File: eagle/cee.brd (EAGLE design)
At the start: 50 x 80 mm, 51 parts, among them IC1 IC1, J1 SOLDERJUMPERNC2

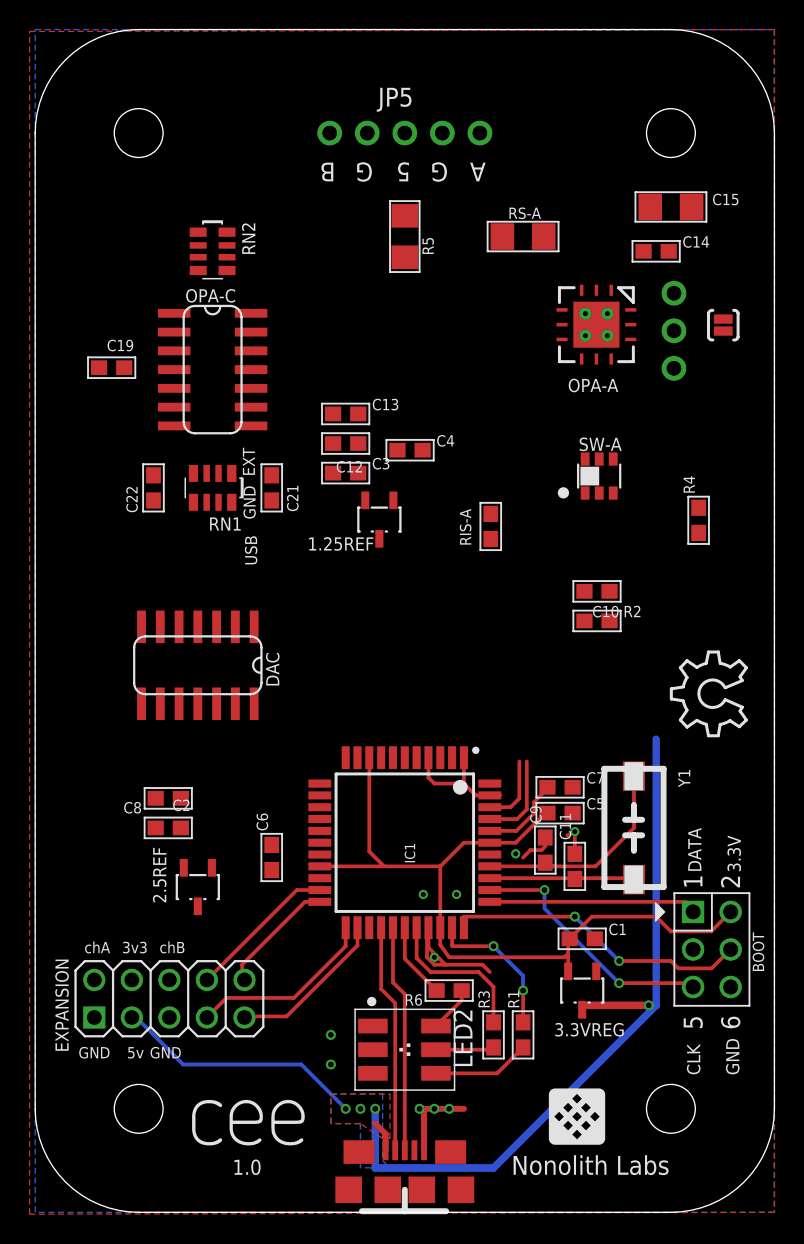
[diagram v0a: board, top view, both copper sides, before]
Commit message: Move output header 1mm inward so it doesn't go beyond acrylic.
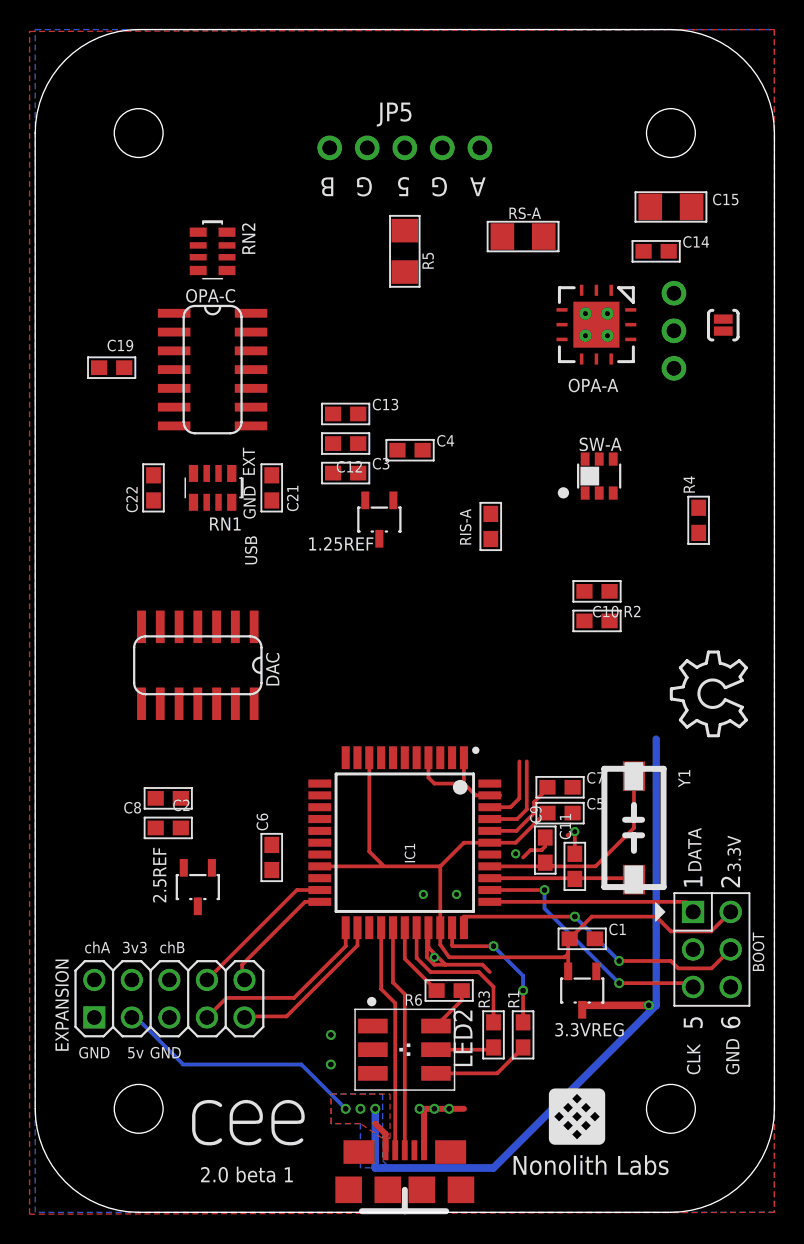
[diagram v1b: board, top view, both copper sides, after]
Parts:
- moved JP5 1.00 mm to (25.0, 72.0)
- moved R5 1.00 mm to (25.0, 65.0)
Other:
- board text added: "2.0 beta 1"
- board text removed: "1.0"
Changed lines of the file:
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@@
 <text x="36.0238" y="55.482" size="0.889" layer="25" font="vector" ratio="12">OPA-A</text>
 <text x="32.2072" y="2.54" size="1.27" layer="25" font="vector" ratio="12">Nonolith Labs</text>
-<text x="20.32" y="71" size="1.27" layer="25" font="vector" ratio="12" rot="SR180">B</text>
-<text x="30.48" y="71" size="1.27" layer="25" font="vector" ratio="12" rot="SR180">A</text>
+<text x="20.32" y="70" size="1.27" layer="25" font="vector" ratio="12" rot="SR180">B</text>
+<text x="30.48" y="70" size="1.27" layer="25" font="vector" ratio="12" rot="SR180">A</text>
 <text x="14.859" y="49.784" size="0.8128" layer="21" rot="R90">EXT</text>
 <text x="15.0114" y="43.7388" size="0.8128" layer="21" rot="R90">USB</text>
@@
 <text x="5.08" y="11.176" size="0.762" layer="25" font="vector" ratio="11" rot="R180">GND</text>
 <text x="7.366" y="11.176" size="0.762" layer="25" font="vector" ratio="11" rot="R180">5v</text>
-<text x="13.335" y="2.54" size="1.016" layer="25" font="vector" ratio="12">1.0</text>
-<text x="22.86" y="71" size="1.27" layer="25" font="vector" ratio="12" rot="SR180">G</text>
-<text x="25.4" y="71" size="1.27" layer="25" font="vector" ratio="12" rot="SR180">5</text>
-<text x="27.94" y="71" size="1.27" layer="25" font="vector" ratio="12" rot="SR180">G</text>
+<text x="14.335" y="2.54" size="1.016" layer="25" font="vector" ratio="12" align="center">2.0 beta 1</text>
+<text x="22.86" y="70" size="1.27" layer="25" font="vector" ratio="12" rot="SR180">G</text>
+<text x="25.4" y="70" size="1.27" layer="25" font="vector" ratio="12" rot="SR180">5</text>
+<text x="27.94" y="70" size="1.27" layer="25" font="vector" ratio="12" rot="SR180">G</text>
 <text x="9.906" y="11.176" size="0.762" layer="25" font="vector" ratio="11" rot="R180">GND</text>
 </plain>
@@
 <attribute name="NAME" x="14" y="67" size="0.889" layer="25" font="vector" ratio="12" rot="R270"/>
 </element>
-<element name="JP5" library="nonolith" package="1X05_ROUND" value="" x="25" y="73" smashed="yes" rot="R180">
-<attribute name="NAME" x="23.1838" y="74.7928" size="1.27" layer="25" ratio="10"/>
-<attribute name="VALUE" x="31.35" y="76.175" size="1.27" layer="27" rot="R180"/>
-</element>
-<element name="R5" library="nonolith" package="1206" value="15o" x="25" y="66" smashed="yes" rot="R90">
-<attribute name="NAME" x="26.9558" y="64.73" size="0.762" layer="25" font="vector" ratio="10" rot="R90"/>
+<element name="JP5" library="nonolith" package="1X05_ROUND" value="" x="25" y="72" smashed="yes" rot="R180">
+<attribute name="NAME" x="23.1838" y="73.7928" size="1.27" layer="25" ratio="10"/>
+<attribute name="VALUE" x="31.35" y="75.175" size="1.27" layer="27" rot="R180"/>
+</element>
+<element name="R5" library="nonolith" package="1206" value="15o" x="25" y="65" smashed="yes" rot="R90">
+<attribute name="NAME" x="26.9558" y="63.73" size="0.762" layer="25" font="vector" ratio="10" rot="R90"/>
 </element>
 <element name="CN1" library="nonolith" package="USB-MICROB" value="" x="25" y="1.524"/>
@@
 <contactref element="RN2" pad="1"/>
 <contactref element="JP5" pad="1"/>
-<wire x1="31.6" y1="66" x2="30.08" y2="73" width="0" layer="19" extent="1-1"/>
-<wire x1="11.025" y1="66.295" x2="30.08" y2="73" width="0" layer="19" extent="1-1"/>
+<wire x1="31.6" y1="66" x2="30.08" y2="72" width="0" layer="19" extent="1-1"/>
+<wire x1="11.025" y1="66.295" x2="30.08" y2="72" width="0" layer="19" extent="1-1"/>
 <wire x1="11.025" y1="65.4" x2="11.025" y2="66.295" width="0" layer="19" extent="1-1"/>
 <wire x1="3.997" y1="15.718" x2="11.025" y2="65.4" width="0" layer="19" extent="1-1"/>
@@
 <contactref element="RN2" pad="3"/>
 <contactref element="JP5" pad="5"/>
-<wire x1="11.025" y1="64.6" x2="19.92" y2="73" width="0" layer="19" extent="1-1"/>
+<wire x1="11.025" y1="64.6" x2="19.92" y2="72" width="0" layer="19" extent="1-1"/>
 <wire x1="9.077" y1="15.718" x2="11.025" y2="64.6" width="0" layer="19" extent="1-1"/>
 </signal>
@@
 <wire x1="43.2052" y1="62.165" x2="40.285" y2="61.04" width="0" layer="19" extent="1-1"/>
 <wire x1="46.542" y1="60.4187" x2="43.2052" y2="62.165" width="0" layer="19" extent="1-1"/>
-<wire x1="25" y1="64.6" x2="38.96" y2="62.365" width="0" layer="19" extent="1-1"/>
+<wire x1="25" y1="63.6" x2="38.96" y2="62.365" width="0" layer="19" extent="1-1"/>
 </signal>
 <signal name="BOOTLOAD">
@@
 <contactref element="JP5" pad="3"/>
 <contactref element="R5" pad="2"/>
-<wire x1="25" y1="67.4" x2="25" y2="73" width="0" layer="19" extent="1-1"/>
+<wire x1="25" y1="66.4" x2="25" y2="72" width="0" layer="19" extent="1-1"/>
 </signal>
 <signal name="N$3">

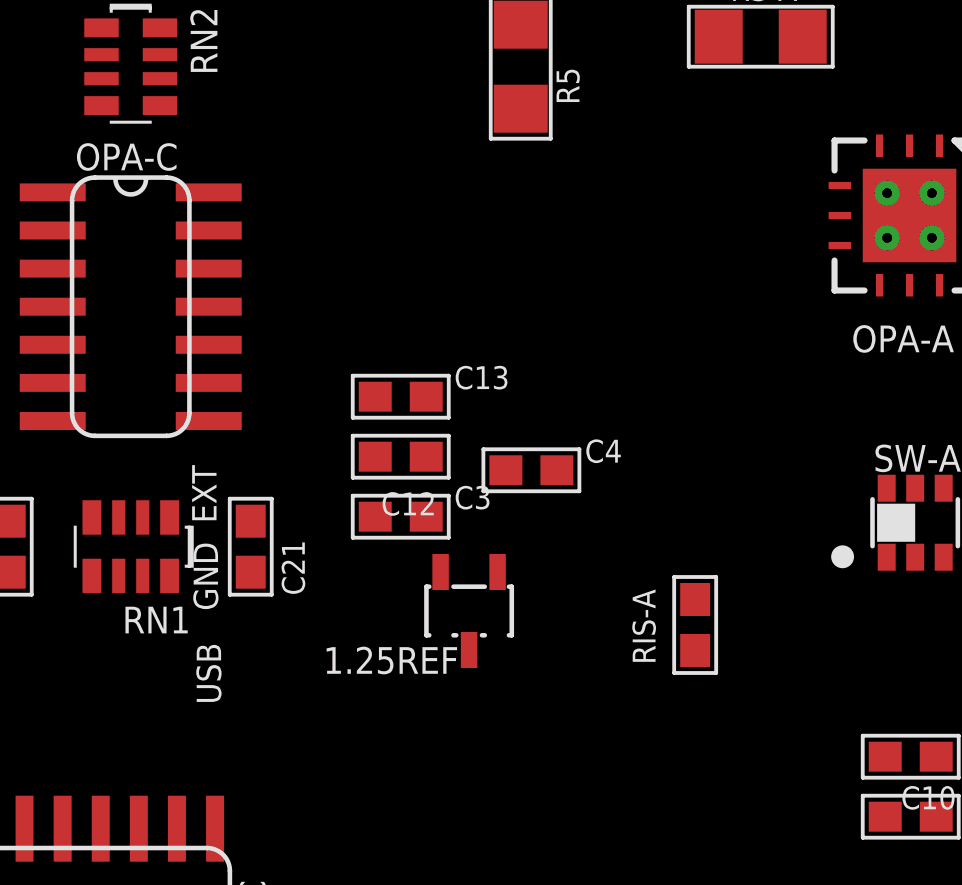
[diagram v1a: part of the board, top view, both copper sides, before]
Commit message: added INA21x
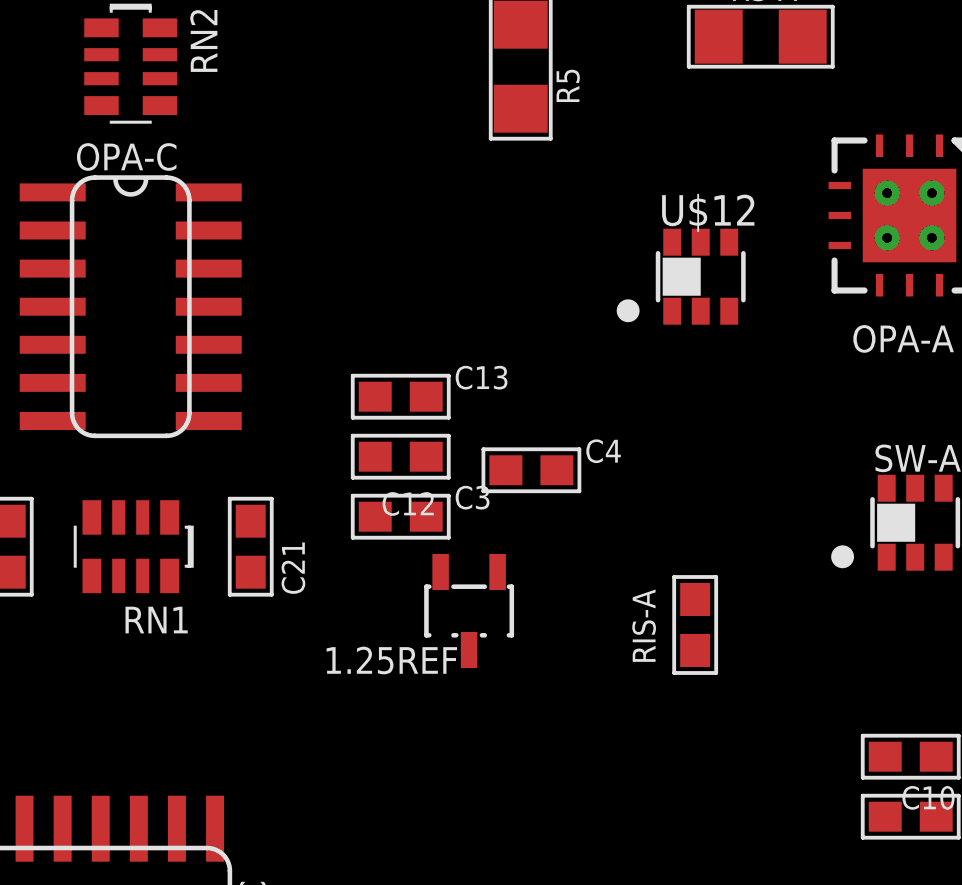
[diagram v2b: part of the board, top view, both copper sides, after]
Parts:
- added U$12: INA213, nonolith:SOT23-6
- C10: value 1nF -> DNI
- R2: value 10ko -> DNI
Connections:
- new net N$13: JP5.5
- net 1.25VREF: now also U$12.1
- net 5V: now also U$12.3
- net GND: now also U$12.2
- net SMU-A: now also U$12.4
- net SMU-B: no longer JP5.5
- net VO-A: now also U$12.5
- net VS-A: now also U$12.6
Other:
- board text removed: "EXT"
- board text removed: "USB"
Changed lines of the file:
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@@
 <?xml version="1.0" encoding="utf-8"?>
 <!DOCTYPE eagle SYSTEM "eagle.dtd">
-<eagle version="6.1">
+<eagle version="6.3">
 <drawing>
 <settings>
@@
 <text x="20.32" y="70" size="1.27" layer="25" font="vector" ratio="12" rot="SR180">B</text>
 <text x="30.48" y="70" size="1.27" layer="25" font="vector" ratio="12" rot="SR180">A</text>
-<text x="14.859" y="49.784" size="0.8128" layer="21" rot="R90">EXT</text>
-<text x="15.0114" y="43.7388" size="0.8128" layer="21" rot="R90">USB</text>
-<text x="14.9098" y="46.863" size="0.8128" layer="21" rot="R90">GND</text>
 <text x="47.625" y="9.271" size="0.889" layer="25" font="vector" ratio="12" rot="R90">GND</text>
 <text x="44.9834" y="9.271" size="0.889" layer="25" font="vector" ratio="12" rot="R90">CLK</text>
@@
 </class>
 </classes>
-<designrules>
+<designrules name="default">
 <description language="de">&lt;b&gt;EAGLE Design Rules&lt;/b&gt;
 &lt;p&gt;
@@
 <attribute name="VALUE" x="35.0188" y="12.1298" size="0.762" layer="27" ratio="12"/>
 </element>
-<element name="R2" library="nonolith" package="0603" value="10ko" x="38" y="40"/>
-<element name="C10" library="nonolith" package="0603" value="1nF" x="38" y="42" smashed="yes" rot="R180">
+<element name="R2" library="nonolith" package="0603" value="DNI" x="38" y="40"/>
+<element name="C10" library="nonolith" package="0603" value="DNI" x="38" y="42" smashed="yes" rot="R180">
 <attribute name="NAME" x="37.6698" y="40.2474" size="0.762" layer="25" font="vector" ratio="10"/>
 </element>
@@
 <element name="R3" library="nonolith" package="0603" value="0" x="31" y="12" rot="R90"/>
 <element name="R6" library="nonolith" package="0603" value="0" x="28" y="15" rot="R180"/>
+<element name="U$12" library="nonolith" package="SOT23-6" value="INA213" x="31" y="58"/>
 </elements>
 <signals>
@@
 <wire x1="10" y1="10" x2="18" y2="10" width="0.254" layer="16"/>
 <wire x1="18" y1="10" x2="21" y2="7" width="0.254" layer="16"/>
+<contactref element="U$12" pad="3"/>
 <wire x1="43.2052" y1="57.085" x2="46.542" y2="59.6051" width="0" layer="19" extent="1-1"/>
 <wire x1="38.148" y1="50.949" x2="43.2052" y2="57.085" width="0" layer="19" extent="1-1"/>
-<wire x1="24.505" y1="51.548" x2="38.148" y2="50.949" width="0" layer="19" extent="1-1"/>
+<wire x1="31.95" y1="56.85" x2="38.148" y2="50.949" width="0" layer="19" extent="1-1"/>
+<wire x1="24.505" y1="51.548" x2="31.95" y2="56.85" width="0" layer="19" extent="1-1"/>
 <wire x1="24.229" y1="48.1574" x2="24.505" y2="51.548" width="0" layer="19" extent="1-1"/>
 <wire x1="14.81" y1="39.6" x2="24.229" y2="48.1574" width="0" layer="19" extent="1-1"/>
@@
 <contactref element="JP5" pad="4"/>
 <contactref element="EXPANSION" pad="5"/>
-<contactref element="C4" pad="1"/>
 <polygon width="0.4064" layer="16" isolate="0.3048" rank="3">
 <vertex x="0" y="80"/>
@@
 <via x="26.25" y="21.5" extent="1-16" drill="0.3302" shape="octagon"/>
 <via x="28.5" y="21.5" extent="1-16" drill="0.3302" shape="octagon"/>
+<contactref element="U$12" pad="2"/>
+<contactref element="C4" pad="1"/>
 </signal>
 <signal name="PDI-DATA">
@@
 <contactref element="RN2" pad="1"/>
 <contactref element="JP5" pad="1"/>
+<contactref element="U$12" pad="4"/>
 <wire x1="31.6" y1="66" x2="30.08" y2="72" width="0" layer="19" extent="1-1"/>
+<wire x1="31.95" y1="59.15" x2="31.6" y2="66" width="0" layer="19" extent="1-1"/>
 <wire x1="11.025" y1="66.295" x2="30.08" y2="72" width="0" layer="19" extent="1-1"/>
 <wire x1="11.025" y1="65.4" x2="11.025" y2="66.295" width="0" layer="19" extent="1-1"/>
@@
 <contactref element="RS-A" pad="1"/>
 <contactref element="C10" pad="2"/>
+<contactref element="U$12" pad="5"/>
 <wire x1="37.96" y1="62.365" x2="36.96" y2="62.365" width="0" layer="19" extent="1-1"/>
 <wire x1="34.4" y1="66" x2="36.96" y2="62.365" width="0" layer="19" extent="1-1"/>
-<wire x1="37.15" y1="42" x2="36.96" y2="62.365" width="0" layer="19" extent="1-1"/>
+<wire x1="31" y1="59.15" x2="36.96" y2="62.365" width="0" layer="19" extent="1-1"/>
+<wire x1="37.15" y1="42" x2="31" y2="59.15" width="0" layer="19" extent="1-1"/>
 </signal>
 <signal name="VIN-A">
@@
 <wire x1="32.6" y1="26.6" x2="33.25" y2="27.25" width="0.254" layer="1"/>
 <wire x1="33.25" y1="27.25" x2="33.25" y2="30.5" width="0.254" layer="1"/>
+<contactref element="U$12" pad="6"/>
+<wire x1="37.15" y1="40" x2="30.05" y2="59.15" width="0" layer="19" extent="1-1"/>
 <wire x1="33.25" y1="30.5" x2="37.15" y2="40" width="0" layer="19" extent="1-1"/>
 </signal>
@@
 <contactref element="EXPANSION" pad="6"/>
 <contactref element="RN2" pad="3"/>
-<contactref element="JP5" pad="5"/>
-<wire x1="11.025" y1="64.6" x2="19.92" y2="72" width="0" layer="19" extent="1-1"/>
 <wire x1="9.077" y1="15.718" x2="11.025" y2="64.6" width="0" layer="19" extent="1-1"/>
 </signal>
@@
 <wire x1="26.6" y1="29.4" x2="27" y2="29" width="0.254" layer="1"/>
 <wire x1="27" y1="29" x2="29" y2="29" width="0.254" layer="1"/>
+<contactref element="U$12" pad="1"/>
+<wire x1="20.15" y1="54" x2="30.05" y2="56.85" width="0" layer="19" extent="1-1"/>
 <wire x1="20.15" y1="52" x2="20.15" y2="54" width="0" layer="19" extent="1-1"/>
 <wire x1="20.15" y1="50" x2="20.15" y2="52" width="0" layer="19" extent="1-1"/>
@@
 <wire x1="14.229" y1="13.25" x2="14.157" y2="13.178" width="0.254" layer="1"/>
 </signal>
+<signal name="N$13">
+<contactref element="JP5" pad="5"/>
+</signal>
 </signals>
